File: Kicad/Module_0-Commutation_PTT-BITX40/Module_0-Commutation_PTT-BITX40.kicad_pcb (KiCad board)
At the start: 2 copper layers, 125 x 50 mm, 41 parts, among them J1 Conn_01x02, J10 Conn_Coaxial, J11 Conn_Coaxial, J12 Conn_01x02, J13 Conn_01x02, J14 Conn_01x02, J15 Conn_01x02, J16 Conn_01x02, J17 Conn_Coaxial, J18 Conn_01x03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

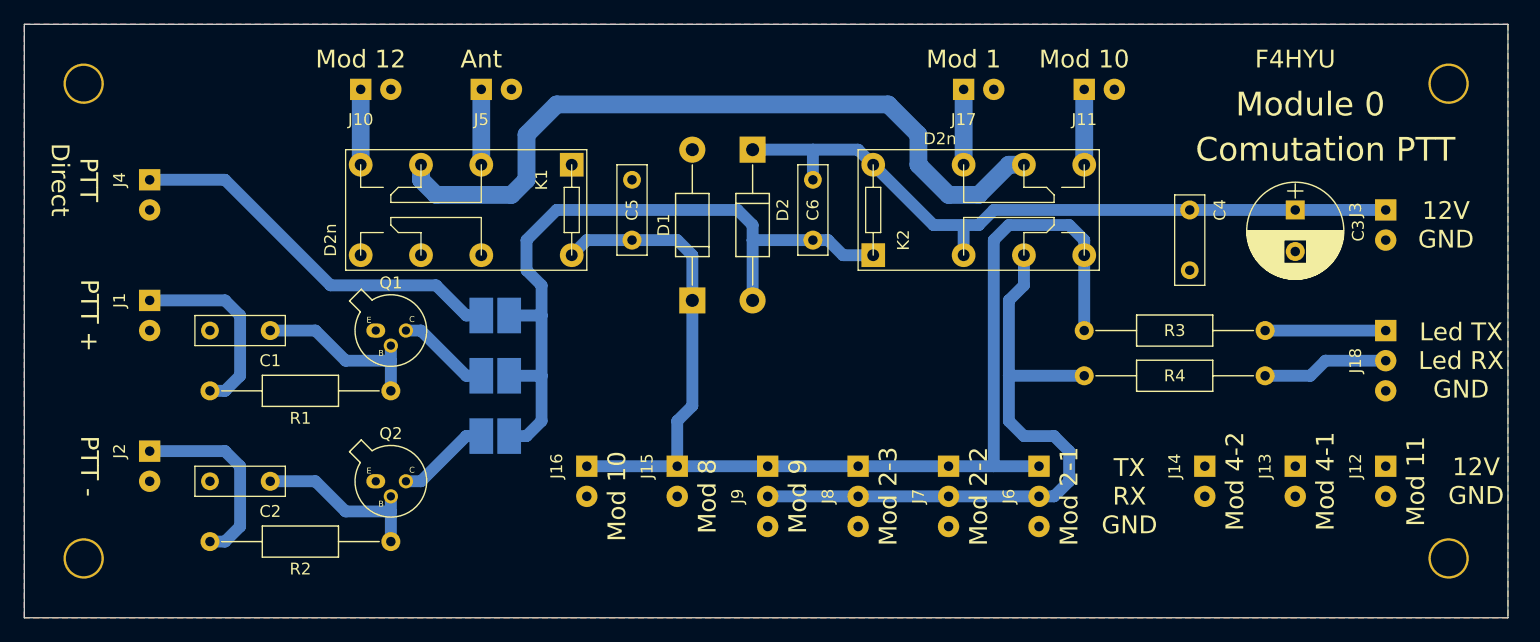
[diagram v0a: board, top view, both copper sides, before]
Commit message: Update missing PTT-
Missing PNP mount PTT- are changed
PTT+ not use GND. Update for the 12V command.
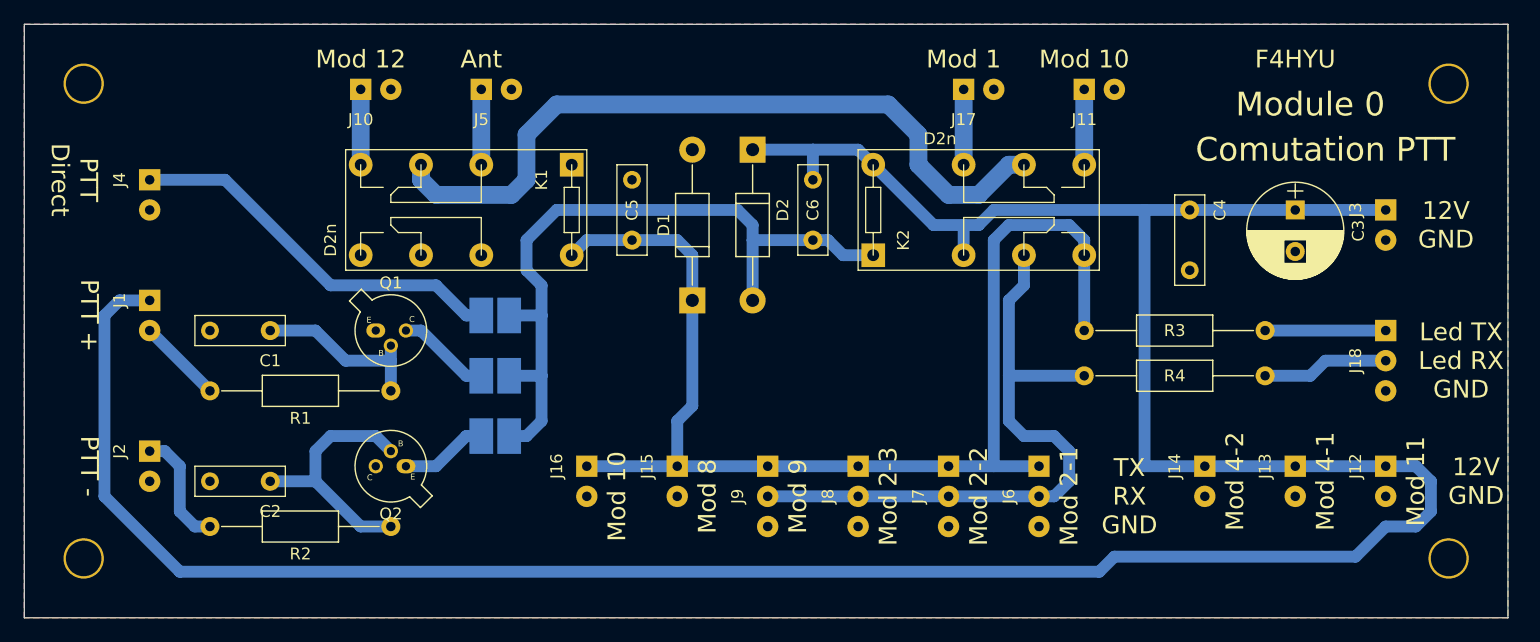
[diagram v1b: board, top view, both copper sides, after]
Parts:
- moved Q2 2.84 mm to (57.1, 62.2), turned to 180 degrees
- moved R2 1.27 mm to (55.9, 67.3)
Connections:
- J1 pad 1: Net-(J1-Pad1) -> 12V
- J1 pad 2: GND -> Net-(J1-Pad2)
- Q2 pad 2: Net-(Q2-Pad2) -> GND
- Q2 pad 3: GND -> Net-(Q2-Pad3)
- R1 pad 2: Net-(J1-Pad1) -> Net-(J1-Pad2)
- SW3 pad 1: Net-(Q2-Pad2) -> Net-(Q2-Pad3)
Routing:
- net 12V: track 61.6 -> 246.4 mm
- net Net-(J1-Pad1): track 16.3 -> 0.00 mm
- net Net-(Q2-Pad2): track 7.93 -> 0.00 mm
- net Net-(Q2-Pad3): track 0.00 -> 7.40 mm
- net Net-(J1-Pad2): track 0.00 -> 7.18 mm
- net Net-(C2-Pad1): track 15.0 -> 21.7 mm
- net Net-(J2-Pad1): track 16.3 -> 9.94 mm
